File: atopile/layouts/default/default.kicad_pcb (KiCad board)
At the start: 2 copper layers, 78 x 60 mm, 86 parts

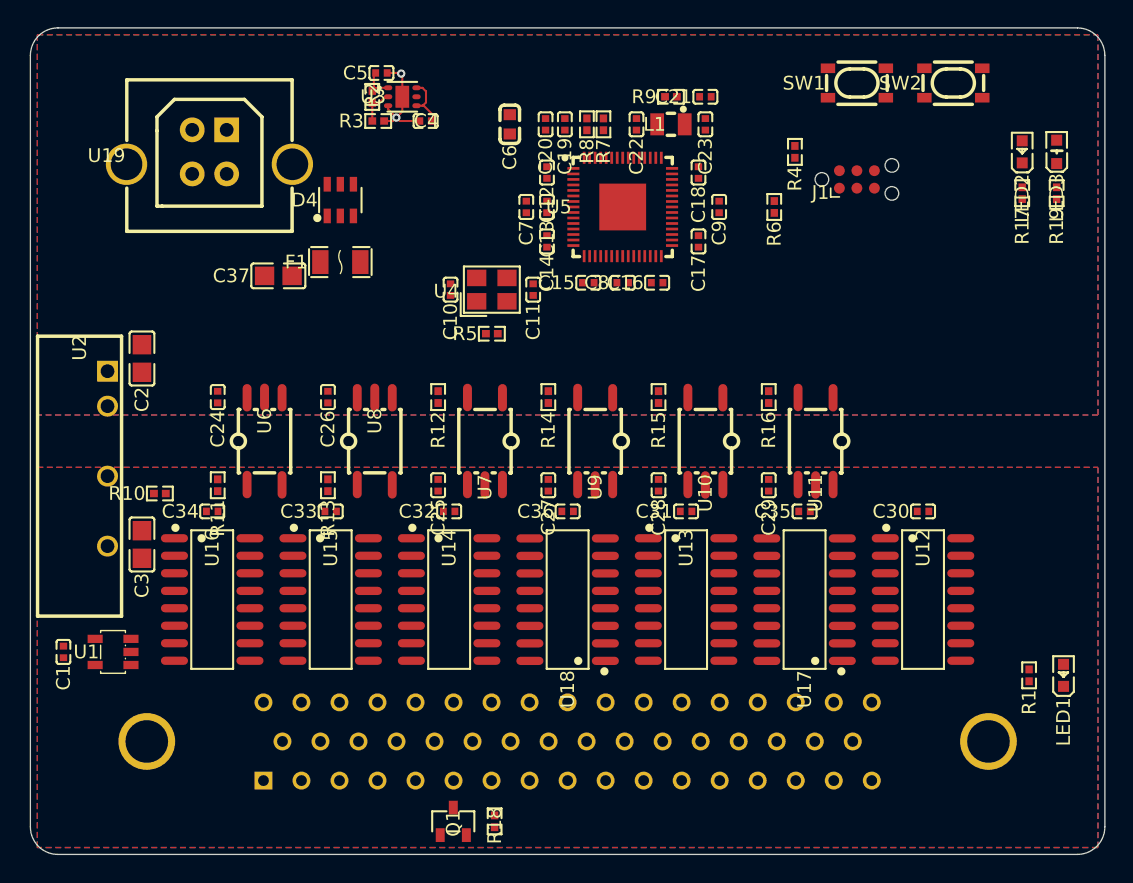
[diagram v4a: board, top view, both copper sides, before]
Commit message: atopile: 4-layer board with inner GND/supply planes and plane via drops
- place_components.py: In1.Cu (GND | GND_ISO) and In2.Cu (+3V3 | +5V_ISO)
  plane layers, JLCPCB 7628 stack-up, barrier keep-out on all four layers,
  no outer pours
- plane_vias.py: stub + via from every SMD pad on a plane net to its plane
  (148 vias, DRC clean), so the autorouter only routes signals
- export_dsn.py / import_routing.py: Freerouting round trip that keeps the
  layout in atopile's file format
- export_pcb.py: inner layers in the gerbers and prints

Fab outputs are regenerated once the Freerouting run finishes.

Co-Authored-By: Claude Opus 5.5 <noreply@anthropic.com>
Claude-Session: https://claude.ai/code/session_01NqBEt2iCuw3VMJkgzgPtpr
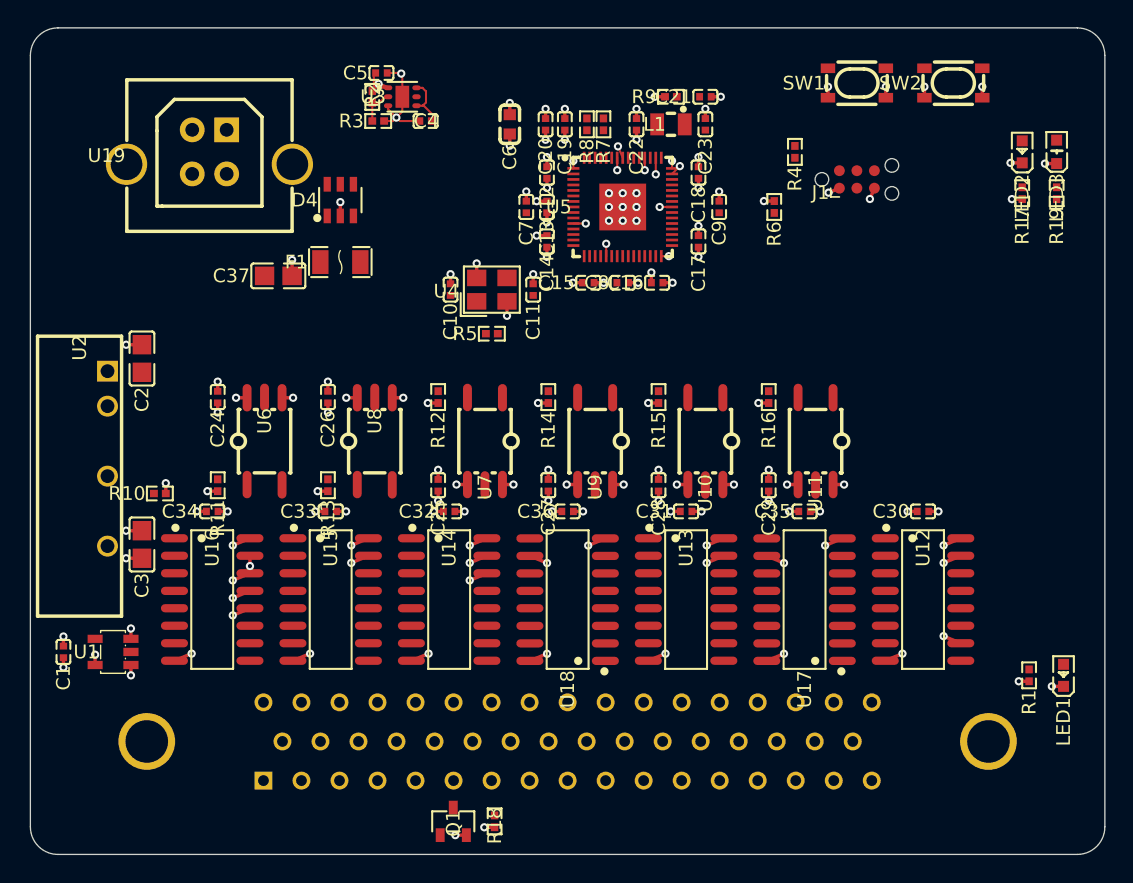
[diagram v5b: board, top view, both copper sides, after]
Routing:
- net GND_ISO: track 0.00 -> 36.3 mm, vias 0 -> 37
- net +5V_ISO: track 0.00 -> 31.4 mm, vias 0 -> 33
- net GND: track 8.09 -> 36.3 mm, vias 2 -> 46
- net +3V3: track 2.74 -> 28.3 mm, vias 0 -> 34
- added copper zone on In2.Cu, net +3V3
- added copper zone on In2.Cu, net +5V_ISO
- added copper zone on In1.Cu, net GND
- added copper zone on In1.Cu, net GND_ISO
- removed copper zone on B.Cu, net GND
- removed copper zone on F.Cu, net GND
- removed copper zone on B.Cu, net GND_ISO
- removed copper zone on F.Cu, net GND_ISO
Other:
- copper layers 2 -> 4

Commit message: atopile: import Freerouting run (4 layers, via drops, 0.2/0.15 mm rules)
Routed by Freerouting 2.1 with only the plane via drops and the LDO block
locked; 2 connections (SCK, LATCH at the RP2354A) still open. Export and
import now lock the same set (plane-net and grouped tracks), so a later
run can rip up and finish the signal routing.

Co-Authored-By: Claude Opus 5.5 <noreply@anthropic.com>
Claude-Session: https://claude.ai/code/session_01NqBEt2iCuw3VMJkgzgPtpr
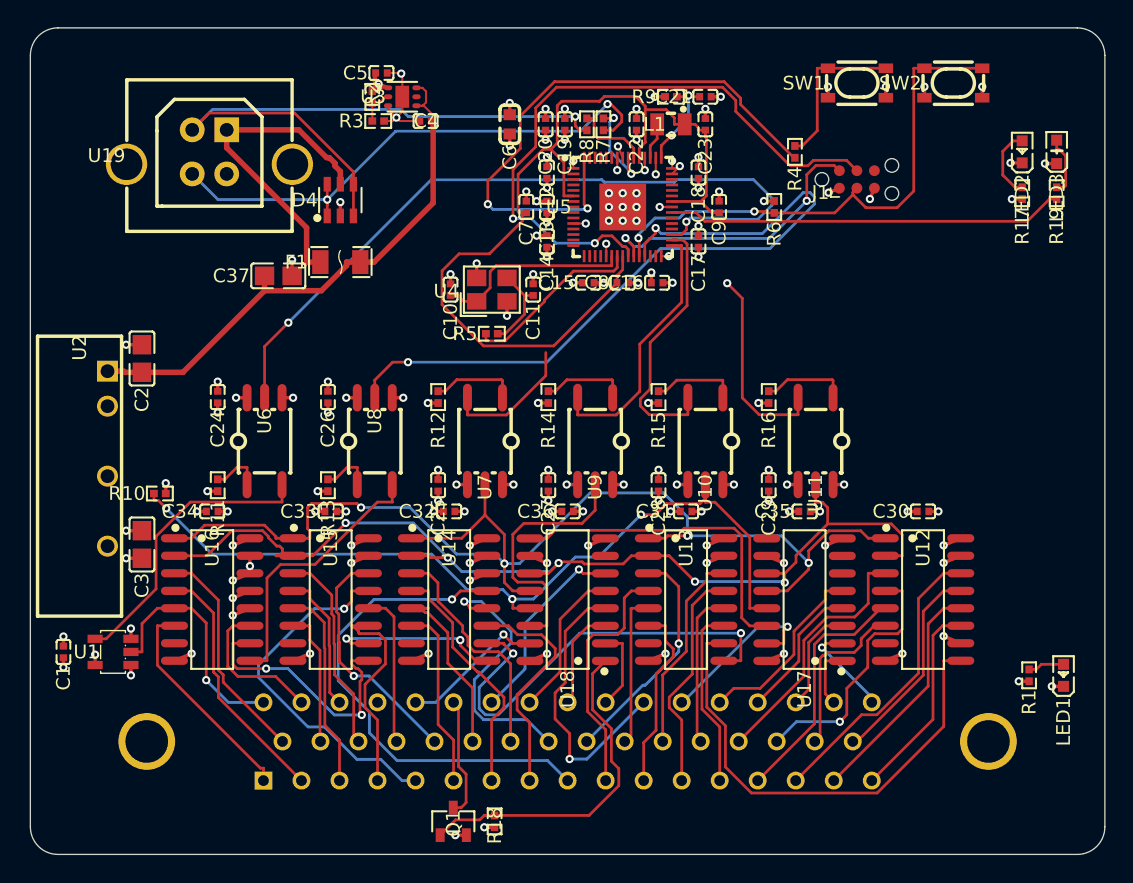
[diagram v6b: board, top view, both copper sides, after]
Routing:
- net LATCH_ISO: track 0.00 -> 86.5 mm, vias 0 -> 4
- net SCK_ISO: track 0.00 -> 74.8 mm, vias 0 -> 5
- net +1V1: track 0.00 -> 68.0 mm
- net OE_N_ISO: track 0.00 -> 60.4 mm, vias 0 -> 3
- net DRDY: track 0.00 -> 55.3 mm, vias 0 -> 2
- net MISO: track 0.00 -> 54.4 mm, vias 0 -> 2
- net DATA_N: track 0.00 -> 47.5 mm, vias 0 -> 1
- net CLK: track 0.00 -> 46.2 mm, vias 0 -> 2
- net QSPI_SS: track 0.00 -> 42.1 mm, vias 0 -> 2
- net DATA_P: track 0.00 -> 39.5 mm, vias 0 -> 2
- net N_RESET: track 0.00 -> 38.2 mm, vias 0 -> 2
- net +5V: track 3.86 -> 40.1 mm
- net SKB09_D4_1: track 0.00 -> 36.0 mm, vias 0 -> 1
- net SI_CHAIN_4: track 0.00 -> 35.4 mm
- net SI_CHAIN_3: track 0.00 -> 32.2 mm, vias 0 -> 2
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
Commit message: atopile: keep plane via drops out of IC pins' escape zones
plane_vias.py penalises via spots within 1.5 mm of another net's IC pin on
its outward side. A decoupling cap's via under RP2354A pins 27/28 had
blocked SCK and LATCH. Layout reset to the new via drops (unrouted) for
the next Freerouting run.

Co-Authored-By: Claude Opus 5.5 <noreply@anthropic.com>
Claude-Session: https://claude.ai/code/session_01NqBEt2iCuw3VMJkgzgPtpr
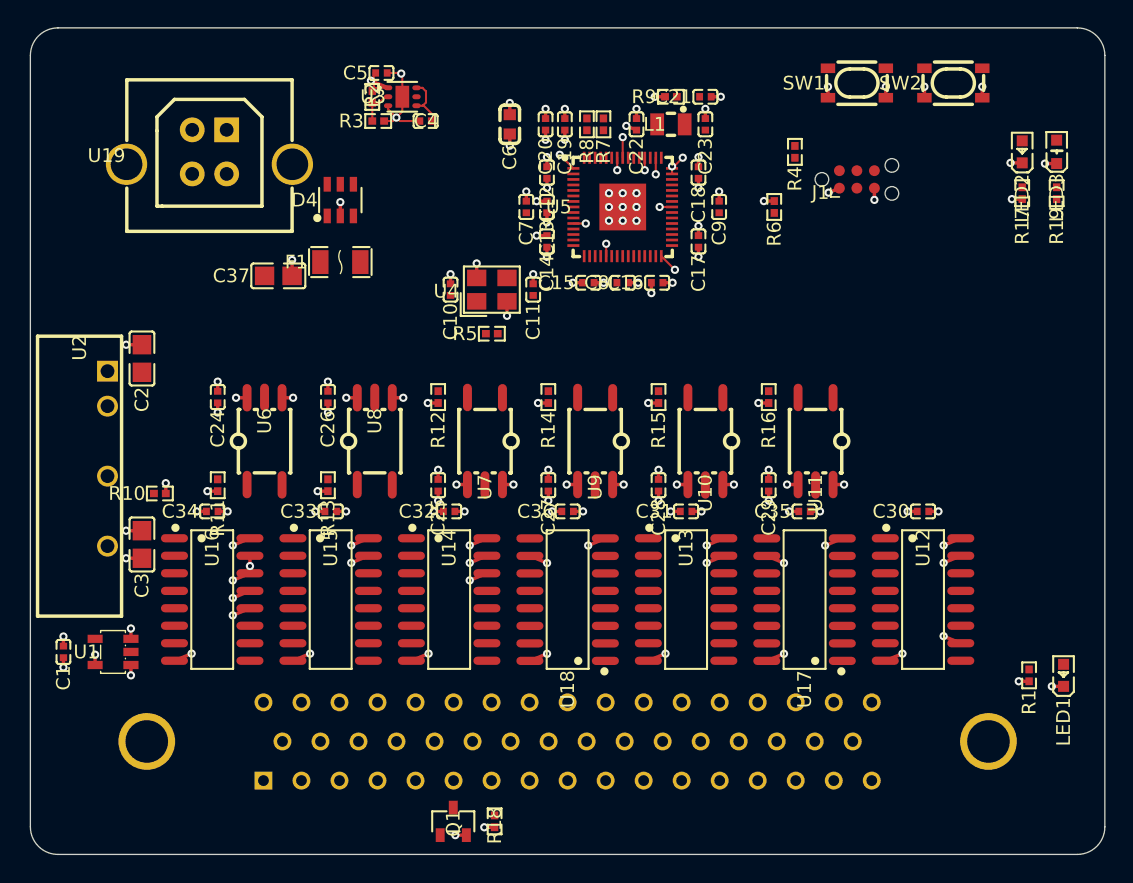
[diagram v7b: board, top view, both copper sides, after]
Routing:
- net LATCH_ISO: track 86.5 -> 0.00 mm, vias 4 -> 0
- net SCK_ISO: track 74.8 -> 0.00 mm, vias 5 -> 0
- net +1V1: track 68.0 -> 0.00 mm
- net OE_N_ISO: track 60.4 -> 0.00 mm, vias 3 -> 0
- net DRDY: track 55.3 -> 0.00 mm, vias 2 -> 0
- net MISO: track 54.4 -> 0.00 mm, vias 2 -> 0
- net DATA_N: track 47.5 -> 0.00 mm, vias 1 -> 0
- net CLK: track 46.2 -> 0.00 mm, vias 2 -> 0
- net QSPI_SS: track 42.1 -> 0.00 mm, vias 2 -> 0
- net DATA_P: track 39.5 -> 0.00 mm, vias 2 -> 0
- net N_RESET: track 38.2 -> 0.00 mm, vias 2 -> 0
- net +5V: track 40.1 -> 3.86 mm
- net SKB09_D4_1: track 36.0 -> 0.00 mm, vias 1 -> 0
- net SI_CHAIN_4: track 35.4 -> 0.00 mm
- net SI_CHAIN_3: track 32.2 -> 0.00 mm, vias 2 -> 0
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
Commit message: atopile: import Freerouting run 5; finish_routes.py clean-up and rip-up
- layout: run 5 routing (patched Freerouting 2.1, escape-aware via
  drops); KiCad finds 8 nets still split, mostly at the RP2354A
- finish_routes.py: removes dangling signal vias/tracks first, aligns
  its grid to absolute 0.05 mm (fine-pitch escapes), retries failed nets
  first, and rips up conflicting signal segments when a net still fails
- import_routing.py: tracks_of() helper shared with finish_routes.py

Co-Authored-By: Claude Opus 5.5 <noreply@anthropic.com>
Claude-Session: https://claude.ai/code/session_01NqBEt2iCuw3VMJkgzgPtpr
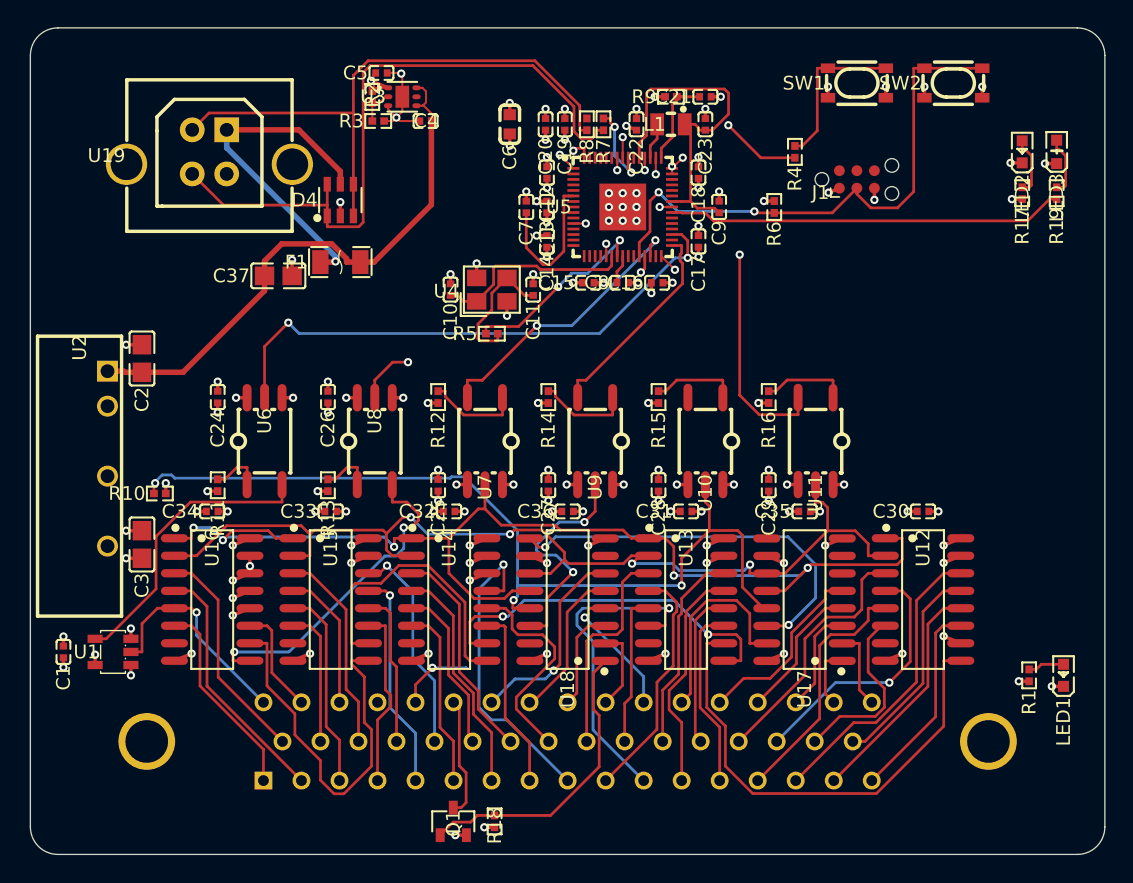
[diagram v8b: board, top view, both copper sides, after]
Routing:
- net LATCH_ISO: track 0.00 -> 82.7 mm, vias 0 -> 5
- net SCK_ISO: track 0.00 -> 74.7 mm, vias 0 -> 4
- net OE_N_ISO: track 0.00 -> 65.0 mm, vias 0 -> 3
- net DATA_P: track 0.00 -> 48.7 mm
- net DATA_N: track 0.00 -> 42.9 mm
- net N_RESET: track 0.00 -> 40.4 mm, vias 0 -> 2
- net DRDY: track 0.00 -> 40.3 mm, vias 0 -> 2
- net +1V1: track 0.00 -> 38.9 mm
- net +5V: track 3.86 -> 41.3 mm
- net SI_CHAIN_4: track 0.00 -> 35.4 mm
- net SO_CHAIN_1: track 0.00 -> 29.0 mm, vias 0 -> 2
- net STATUS_LED: track 0.00 -> 28.8 mm
- net SI_CHAIN_1: track 0.00 -> 27.2 mm
- net SI_CHAIN_3: track 0.00 -> 27.1 mm, vias 0 -> 2
- net VBUS: track 0.00 -> 24.4 mm, vias 0 -> 1
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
